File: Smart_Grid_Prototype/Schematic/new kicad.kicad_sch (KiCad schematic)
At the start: 70 parts, among them J1 EXT_POW, J2 24VAC _LOAD, J3 AC_INPUT, J4 DC_LOAD, J5 POW_SHARE, Q1 BD139, Q2 BD139, Q3 BD139, Q4 BD139, Q5 BD139, Q6 BD139, Q7 BD139, U1 ZC563900, U10 MODERATE_V, U11 HIGH_V, U12 PC817, U13 PC817, U14 PC817, U15 PC817, U16 PC817, U2 CKT_1_POWER_CON, U3 CKT_1_POWER_CON, U4 MIN_V, U5 LM7824_TO220, U6 MODERATE_V, U7 PC817, U8 LM317_TO-220, U9 MIN_V

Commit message: pcb updated with accrate component names
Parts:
- D1: value 1N5408/RELAY_FWD -> 1N5408/DIODE
- D2: value 1N5408/RELAY-1_FWD -> 1N5408/DIODE
- D3: value GBU4A -> GBU4A/BRIDGE_RECT
- D7: value LOAD_INDICATOR -> LOAD_STATUS
- R11, R2, R4, R5, R6, R7, R9: value 220 -> 220R
- R14: value 1.5kR -> 1.5k
- R15: value 2kR -> 2k
- R23, R24, R26, R3, R31: value 1 -> 1R
- R27: value 150 -> 150R
- U1: value ZC563900 -> ESP8266
- U10, U6: value MODERATE_V -> PC817
- U11: value HIGH_V -> PC817
- U2: value CKT_1_POWER_CON -> RELAY_INT
- U3: value CKT_1_POWER_CON -> RELAY_PS
- U4, U9: value MIN_V -> PC817
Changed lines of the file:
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@@
 			)
 		)
-		(property "Value" "1N5408/RELAY-1_FWD"
+		(property "Value" "1N5408/DIODE"
 			(at 38.608 83.82 90)
 			(effects
@@
 			)
 		)
-		(property "Value" "CKT_1_POWER_CON"
+		(property "Value" "RELAY_PS"
 			(at 77.47 69.85 0)
 			(effects
@@
 			)
 		)
-		(property "Value" "2kR"
+		(property "Value" "2k"
 			(at 176.53 149.86 90)
 			(effects
@@
 			)
 		)
-		(property "Value" "MODERATE_V"
+		(property "Value" "PC817"
 			(at 154.178 131.826 0)
 			(effects
@@
 			)
 		)
-		(property "Value" "1"
+		(property "Value" "1R"
 			(at 238.76 57.1499 0)
 			(effects
@@
 			)
 		)
-		(property "Value" "1N5408/RELAY_FWD"
+		(property "Value" "1N5408/DIODE"
 			(at 33.528 119.38 90)
 			(effects
@@
 			)
 		)
-		(property "Value" "MIN_V"
+		(property "Value" "PC817"
 			(at 154.178 111.506 0)
 			(effects
@@
 			)
 		)
-		(property "Value" "150"
+		(property "Value" "150R"
 			(at 265.43 113.284 0)
 			(effects
@@
 			)
 		)
-		(property "Value" "MODERATE_V"
+		(property "Value" "PC817"
 			(at 156.972 171.704 0)
 			(effects
@@
 			)
 		)
-		(property "Value" "ZC563900"
+		(property "Value" "ESP8266"
 			(at 18.542 142.748 0)
 			(effects
@@
 			)
 		)
-		(property "Value" "1.5kR"
+		(property "Value" "1.5k"
 			(at 176.53 135.89 90)
 			(effects
@@
 			)
 		)
-		(property "Value" "1"
+		(property "Value" "1R"
 			(at 251.46 57.1499 0)
 			(effects
@@
 			)
 		)
-		(property "Value" "220"
+		(property "Value" "220R"
 			(at 144.78 149.86 90)
 			(effects
@@
 			)
 		)
-		(property "Value" "220"
+		(property "Value" "220R"
 			(at 100.838 187.452 90)
 			(effects
@@
 			)
 		)
-		(property "Value" "1"
+		(property "Value" "1R"
 			(at 262.89 57.1499 0)
 			(effects
@@
 			)
 		)
-		(property "Value" "220"
+		(property "Value" "220R"
 			(at 144.78 135.89 90)
 			(effects
@@
 			)
 		)
-		(property "Value" "220"
+		(property "Value" "220R"
 			(at 139.7 189.23 90)
 			(effects
@@
 			)
 		)
-		(property "Value" "1"
+		(property "Value" "1R"
 			(at 274.32 57.1499 0)
 			(effects
@@
 			)
 		)
-		(property "Value" "MIN_V"
+		(property "Value" "PC817"
 			(at 102.108 175.006 0)
 			(effects
@@
 			)
 		)
-		(property "Value" "LOAD_INDICATOR"
+		(property "Value" "LOAD_STATUS"
 			(at 265.938 71.882 0)
 			(effects
@@
 			)
 		)
-		(property "Value" "1"
+		(property "Value" "1R"
 			(at 107.95 119.3799 0)
 			(effects
@@
 			)
 		)
-		(property "Value" "CKT_1_POWER_CON"
+		(property "Value" "RELAY_INT"
 			(at 71.12 105.41 0)
 			(effects
@@
 		(fields_autoplaced yes)
 		(property "Reference" "D3"
-			(at 62.23 29.1398 0)
+			(at 68.58 29.1398 0)
 			(effects
 				(font
@@
 			)
 		)
-		(property "Value" "GBU4A"
-			(at 62.23 31.6798 0)
+		(property "Value" "GBU4A/BRIDGE_RECT"
+			(at 68.58 31.6798 0)
 			(effects
 				(font
@@
 			)
 		)
-		(property "Value" "220"
+		(property "Value" "220R"
 			(at 144.78 109.22 90)
 			(effects
@@
 			)
 		)
-		(property "Value" "HIGH_V"
+		(property "Value" "PC817"
 			(at 154.178 152.146 0)
 			(effects
@@
 			)
 		)
-		(property "Value" "220"
+		(property "Value" "220R"
 			(at 161.29 48.2599 0)
 			(effects
@@
 			)
 		)
-		(property "Value" "220"
+		(property "Value" "220R"
 			(at 165.1 38.0999 0)
 			(effects

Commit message: Modified
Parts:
- renumbered R17 to R16, R18 to R17, R16 to R18
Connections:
- net EXT_POWER: now also U1.15 (VIN)
- no-connect marks 14 -> 13
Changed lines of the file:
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@@
 	)
 	(no_connect
-		(at 24.13 146.05)
-	)
-	(no_connect
 		(at 24.13 171.45)
 	)
@@
 	(wire
 		(pts
+			(xy 19.05 146.05) (xy 24.13 146.05)
+		)
+		(stroke
+			(width 0)
+			(type default)
+		)
+	)
+	(wire
+		(pts
 			(xy 193.04 36.83) (xy 196.85 36.83)
 		)
@@
 		)
 	)
+	(label "EXT_POWER"
+		(at 19.05 146.05 0)
+		(fields_autoplaced yes)
+		(effects
+			(font
+				(size 1.27 1.27)
+			)
+			(justify left bottom)
+		)
+	)
 	(label "1k_R"
 		(at 243.84 118.11 180)
@@
 		(on_board yes)
 		(dnp no)
-		(property "Reference" "R18"
+		(property "Reference" "R17"
 			(at 199.136 39.37 0)
 			(effects
@@
 			(project "new kicad"
 				(path "/e03aa56c-38cd-4df1-a477-6f5e62efd874"
-					(reference "R18")
+					(reference "R17")
 					(unit 1)
 				)
@@
 		(on_board yes)
 		(dnp no)
-		(property "Reference" "R17"
+		(property "Reference" "R16"
 			(at 199.136 26.67 0)
 			(effects
@@
 			(project "new kicad"
 				(path "/e03aa56c-38cd-4df1-a477-6f5e62efd874"
-					(reference "R17")
+					(reference "R16")
 					(unit 1)
 				)
@@
 		(on_board yes)
 		(dnp no)
-		(property "Reference" "R16"
+		(property "Reference" "R18"
 			(at 195.834 87.884 90)
 			(effects
@@
 			(project "new kicad"
 				(path "/e03aa56c-38cd-4df1-a477-6f5e62efd874"
-					(reference "R16")
+					(reference "R18")
 					(unit 1)
 				)

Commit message: updated
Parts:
- renumbered R18 to R16, R16 to R17, R17 to R18
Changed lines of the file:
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@@
 	(wire
 		(pts
-			(xy 19.05 146.05) (xy 24.13 146.05)
-		)
-		(stroke
-			(width 0)
-			(type default)
-		)
-	)
-	(wire
-		(pts
 			(xy 193.04 36.83) (xy 196.85 36.83)
 		)
@@
 		)
 	)
-	(label "EXT_POWER"
-		(at 19.05 146.05 0)
-		(fields_autoplaced yes)
-		(effects
-			(font
-				(size 1.27 1.27)
-			)
-			(justify left bottom)
-		)
-	)
 	(label "1k_R"
 		(at 243.84 118.11 180)
@@
 		)
 	)
+	(label "EXT_POWER"
+		(at 24.13 146.05 180)
+		(effects
+			(font
+				(size 1.27 1.27)
+			)
+			(justify right bottom)
+		)
+	)
 	(label "D5"
 		(at 73.66 158.75 0)
@@
 		(on_board yes)
 		(dnp no)
-		(property "Reference" "R17"
+		(property "Reference" "R18"
 			(at 199.136 39.37 0)
 			(effects
@@
 			(project "new kicad"
 				(path "/e03aa56c-38cd-4df1-a477-6f5e62efd874"
-					(reference "R17")
+					(reference "R18")
 					(unit 1)
 				)
@@
 		(on_board yes)
 		(dnp no)
-		(property "Reference" "R16"
+		(property "Reference" "R17"
 			(at 199.136 26.67 0)
 			(effects
@@
 			(project "new kicad"
 				(path "/e03aa56c-38cd-4df1-a477-6f5e62efd874"
-					(reference "R16")
+					(reference "R17")
 					(unit 1)
 				)
@@
 		(on_board yes)
 		(dnp no)
-		(property "Reference" "R18"
+		(property "Reference" "R16"
 			(at 195.834 87.884 90)
 			(effects
@@
 			(project "new kicad"
 				(path "/e03aa56c-38cd-4df1-a477-6f5e62efd874"
-					(reference "R18")
+					(reference "R16")
 					(unit 1)
 				)

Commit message: not good
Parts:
- added J4: USB4085-GF-A_REVB, USB4085-GF-A_REVB:GCT_USB4085-GF-A_REVB, symbol USB4085-GF-A_REVB:USB4085-GF-A_REVB
- added R1, R2: 5.1k, Resistor_THT:R_Axial_DIN0207_L6.3mm_D2.5mm_P15.24mm_Horizontal, symbol Device:R
- renumbered J4 to J5, J5 to J6, R8 to R10, R9 to R11, R10 to R12, R11 to R13, R12 to R14, R13 to R15, R14 to R16, R15 to R17, R17 to R18, R18 to R19, R16 to R20, R19 to R21, R20 to R22, R21 to R23, R22 to R24, R23 to R25, R24 to R26, R25 to R27, R26 to R28, R27 to R29, R1 to R3, R28 to R30, R29 to R31, R30 to R32, R31 to R33, R2 to R4, R3 to R5, R4 to R6, R5 to R7, R6 to R8, R7 to R9
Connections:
- net EXT_POWER: now also J4.A4 (VBUS), J4.A9 (VBUS), J4.B4 (VBUS), J4.B9 (VBUS)
- net GND: now also J4.A1 (GND), J4.A12 (GND), J4.B1 (GND), J4.B12 (GND), J4.S1 (SHELL), J4.S2 (SHELL), J4.S3 (SHELL), J4.S4 (SHELL), R1.1, R2.1
- new net CC1: J4.A5 (CC1), R1.2
- new net CC2: J4.B5 (CC2), R2.2
- no-connect marks 13 -> 19

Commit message: error
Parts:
- removed J4: USB4085-GF-A_REVB, USB4085-GF-A_REVB:GCT_USB4085-GF-A_REVB, symbol USB4085-GF-A_REVB:USB4085-GF-A_REVB
- added J4: USB_C_Receptacle_PowerOnly_6P, Connector_USB:USB_C_Receptacle_GCT_USB4125-xx-x-0190_6P_TopMnt_Horizontal, symbol Connector:USB_C_Receptacle_PowerOnly_6P
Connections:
- net CC1: now also J4.A5 (CC1)
- net CC2: now also J4.B5 (CC2)
- net GND: now also J4.A12 (GND), J4.B12 (GND), J4.S1 (SHIELD)
- net EXT_POWER renamed VCC
- net VCC: now also J4.A9 (VBUS), J4.B9 (VBUS)
- no-connect marks 19 -> 13

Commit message: Perfect PCB
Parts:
- removed J4: USB_C_Receptacle_PowerOnly_6P, Connector_USB:USB_C_Receptacle_GCT_USB4125-xx-x-0190_6P_TopMnt_Horizontal, symbol Connector:USB_C_Receptacle_PowerOnly_6P
- removed R1, R2: 5.1k, Resistor_THT:R_Axial_DIN0207_L6.3mm_D2.5mm_P15.24mm_Horizontal, symbol Device:R
- added J6: USB_C_Receptacle_PowerOnly_6P, Connector_USB:USB_C_Receptacle_GCT_USB4125-xx-x-0190_6P_TopMnt_Horizontal, symbol Connector:USB_C_Receptacle_PowerOnly_6P
- added R32, R33: 5.1k, Resistor_THT:R_Axial_DIN0207_L6.3mm_D2.5mm_P15.24mm_Horizontal, symbol Device:R
- renumbered J5 to J4, J6 to J5, R3 to R1, R12 to R10, R13 to R11, R14 to R12, R15 to R13, R16 to R14, R17 to R15, R20 to R16, R18 to R17, R19 to R18, R21 to R19, R4 to R2, R22 to R20, R23 to R21, R24 to R22, R25 to R23, R26 to R24, R27 to R25, R28 to R26, R29 to R27, R30 to R28, R31 to R29, R5 to R3, R32 to R30, R33 to R31, R6 to R4, R7 to R5, R8 to R6, R9 to R7, R10 to R8, R11 to R9
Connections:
- net GND: now also J6.A12 (GND), J6.B12 (GND), J6.S1 (SHIELD), R32.1, R33.2
- net VCC: now also J6.A9 (VBUS), J6.B9 (VBUS)
- new net: J6.A5 (CC1), R32.2
- new net: J6.B5 (CC2), R33.1
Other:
- moved on the sheet: C1, C2, C3, C4, D1, D2, D3, D4, D5, D6, D7, J1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

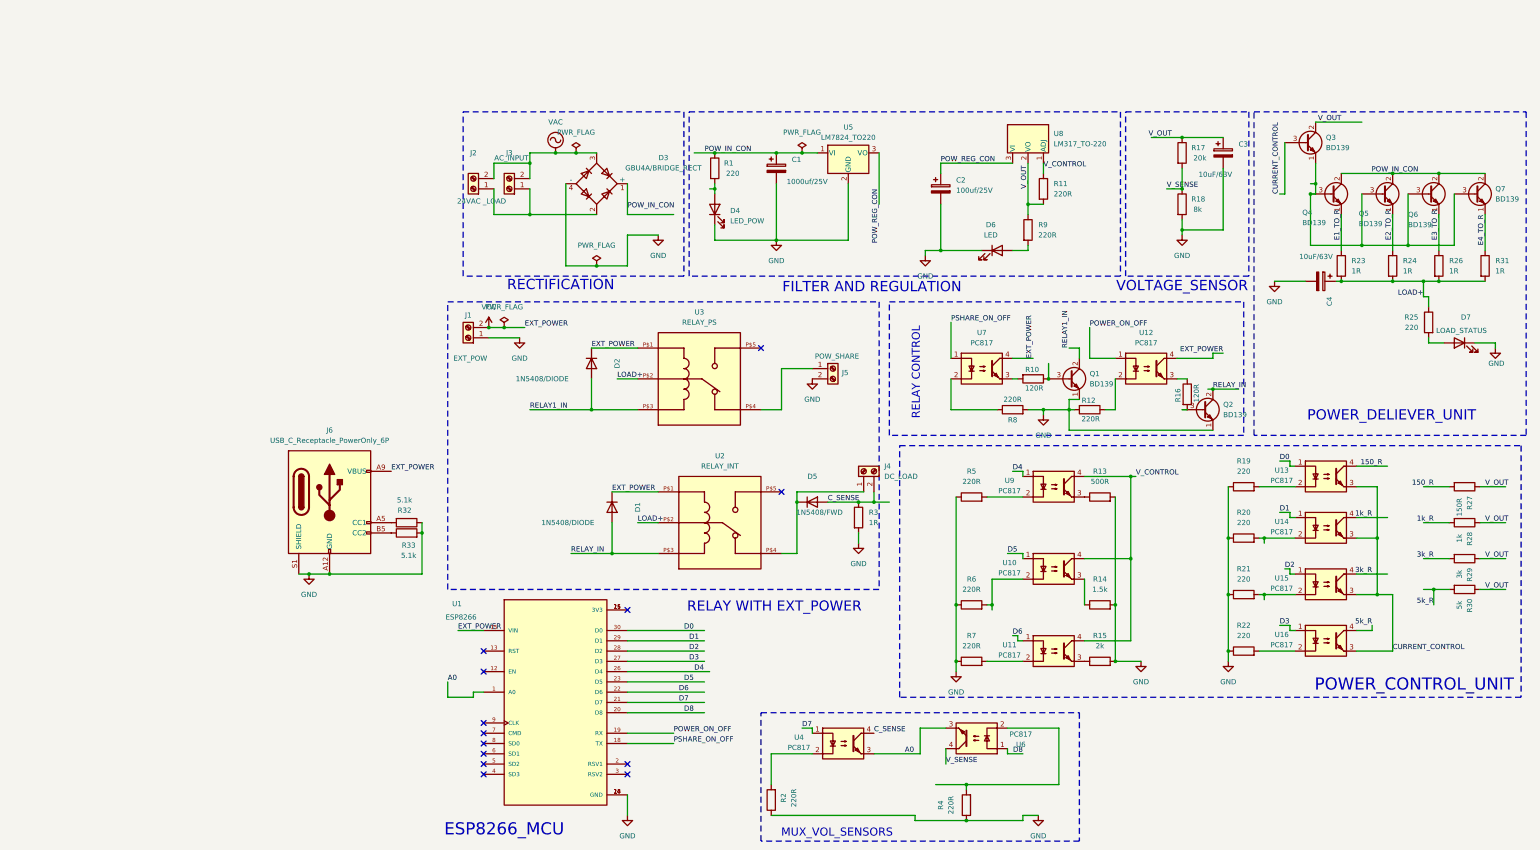
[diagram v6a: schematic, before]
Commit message: ac load switch added
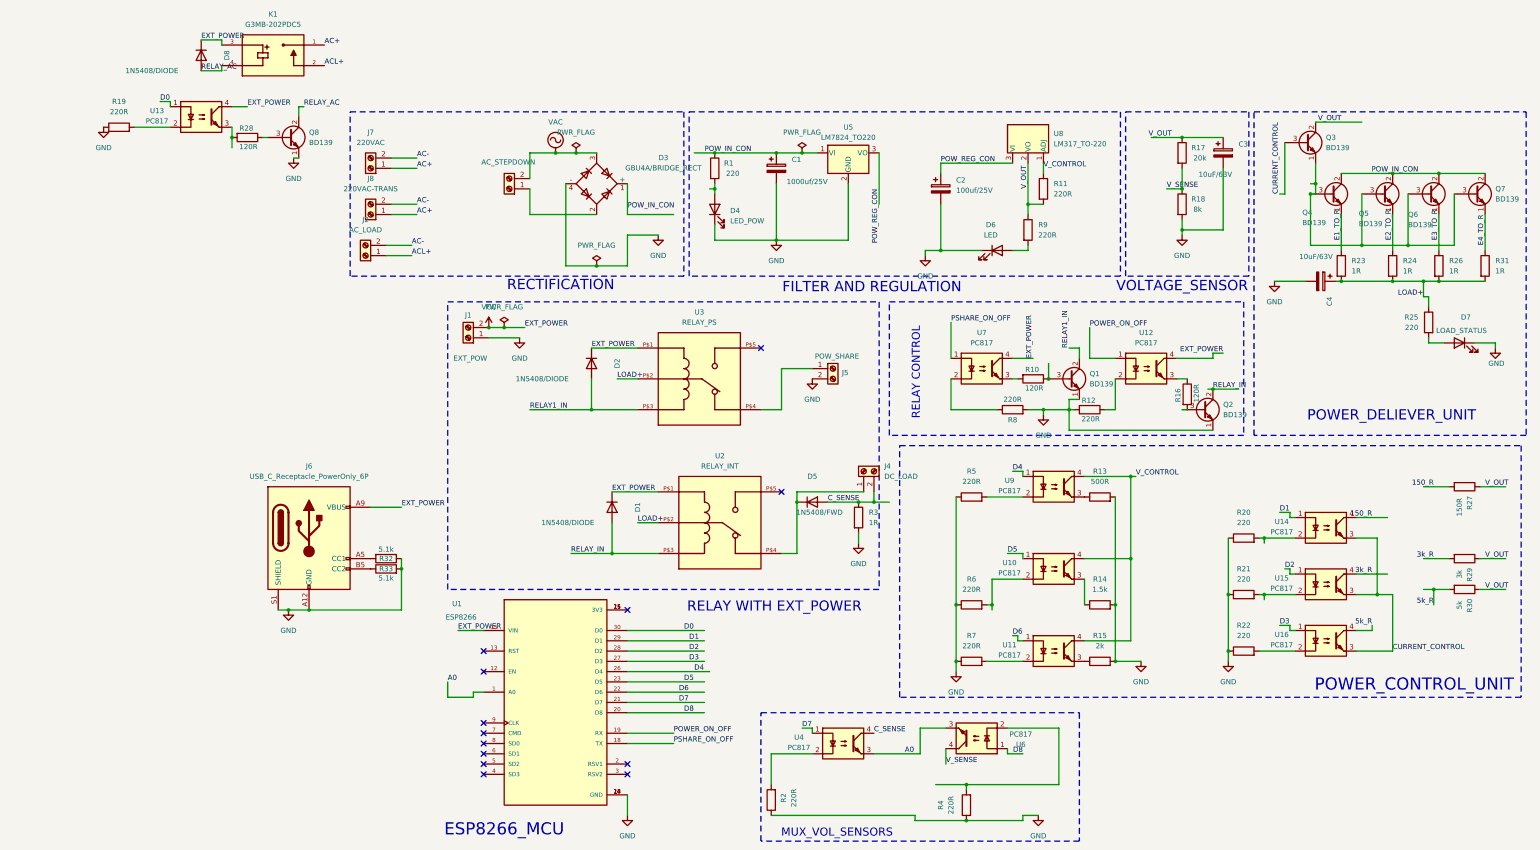
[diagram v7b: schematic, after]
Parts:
- added D8: 1N5408/DIODE, Diode_THT:D_5W_P12.70mm_Horizontal, symbol Device:D
- added J7: 220VAC, TerminalBlock_4Ucon:TerminalBlock_4Ucon_1x02_P3.50mm_Horizontal, symbol Connector:Screw_Terminal_01x02
- added J8: 220VAC-TRANS, TerminalBlock_4Ucon:TerminalBlock_4Ucon_1x02_P3.50mm_Horizontal, symbol Connector:Screw_Terminal_01x02
- added K1: G3MB-202PDC5, Library:RELAY_G3MB-202PDC5, symbol G3MB-202PDC5:G3MB-202PDC5
- added Q8: BD139, Package_TO_SOT_THT:TO-126-3_Vertical, symbol Transistor_BJT:BD139
- J2: value 24VAC _LOAD -> AC_LOAD
- J3: value AC_INPUT -> AC_STEPDOWN
- R19: value 220 -> 220R
- R28: value 1k -> 120R
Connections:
- net 150_R: now also U14.4; no longer U13.4
- net CURRENT_CONTROL: no longer U13.3
- net GND: now also Q8.1 (E)
- net VAC: no longer J2.2 (Pin_2)
- net VCC: now also U13.4, D8.1 (K), K1.3
- net V_OUT: no longer R28.1
- net at D3.2, J3.1 (Pin_1): no longer J2.1 (Pin_1)
- net 1k_R: no longer names the net of R28.2
- net 1k_R: now also U13.3; no longer U14.4
- new net: Q8.3 (B), R28.1
- new net AC+: J7.1 (Pin_1), J8.1 (Pin_1), K1.1
- new net AC-: J2.2 (Pin_2), J7.2 (Pin_2), J8.2 (Pin_2)
- new net ACL+: J2.1 (Pin_1), K1.2
- new net RELAY_AC: D8.2 (A), K1.4, Q8.2 (C)
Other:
- moved on the sheet: J6, R32, R33

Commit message: finalised
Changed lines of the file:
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@@
 	)
 	(junction
+		(at 69.85 166.37)
+		(diameter 0)
+		(color 0 0 0 0)
+	)
+	(junction
 		(at 139.7 81.28)
 		(diameter 0)
@@
 	)
 	(junction
-		(at 68.58 166.37)
-		(diameter 0)
-		(color 0 0 0 0)
-	)
-	(junction
 		(at 328.93 76.2)
 		(diameter 0)
@@
 	(wire
 		(pts
+			(xy 85.09 153.67) (xy 83.82 153.67)
+		)
+		(stroke
+			(width 0)
+			(type default)
+		)
+	)
+	(wire
+		(pts
 			(xy 323.85 68.58) (xy 323.85 77.47)
 		)
@@
 	(wire
 		(pts
+			(xy 85.09 156.21) (xy 83.82 156.21)
+		)
+		(stroke
+			(width 0)
+			(type default)
+		)
+	)
+	(wire
+		(pts
 			(xy 231.14 210.82) (xy 231.14 209.55)
 		)
@@
 	(wire
 		(pts
-			(xy 63.5 166.37) (xy 68.58 166.37)
-		)
-		(stroke
-			(width 0)
-			(type default)
-		)
-	)
-	(wire
-		(pts
 			(xy 294.64 72.39) (xy 284.48 72.39)
 		)
@@
 	(wire
 		(pts
+			(xy 69.85 166.37) (xy 91.44 166.37)
+		)
+		(stroke
+			(width 0)
+			(type default)
+		)
+	)
+	(wire
+		(pts
 			(xy 356.87 100.33) (xy 361.95 100.33)
 		)
@@
 	(wire
 		(pts
-			(xy 83.82 140.97) (xy 91.44 140.97)
+			(xy 85.09 140.97) (xy 91.44 140.97)
 		)
 		(stroke
@@
 	(wire
 		(pts
-			(xy 60.96 166.37) (xy 63.5 166.37)
+			(xy 62.23 166.37) (xy 63.5 166.37)
 		)
 		(stroke
@@
 	(wire
 		(pts
-			(xy 91.44 166.37) (xy 68.58 166.37)
+			(xy 63.5 166.37) (xy 69.85 166.37)
 		)
 		(stroke
@@
 		)
 		(property "Value" "GND"
-			(at 120.65 104.14 0)
+			(at 123.19 100.3299 0)
 			(effects
 				(font
 					(size 1.27 1.27)
 				)
+				(justify left)
 			)
 		)
@@
 		(on_board yes)
 		(dnp no)
-		(fields_autoplaced yes)
 		(property "Reference" "#PWR017"
 			(at 113.03 100.33 0)
@@
 		)
 		(property "Value" "VCC"
-			(at 113.03 91.44 0)
+			(at 113.03 91.694 0)
 			(effects
 				(font
 					(size 1.27 1.27)
 				)
+				(justify left)
 			)
 		)
@@
 		(on_board yes)
 		(dnp no)
-		(fields_autoplaced yes)
 		(property "Reference" "#FLG04"
 			(at 116.84 94.615 0)
@@
 		)
 		(property "Value" "PWR_FLAG"
-			(at 116.84 91.44 0)
+			(at 120.65 92.456 0)
 			(effects
 				(font
 					(size 1.27 1.27)
 				)
+				(justify left)
 			)
 		)
@@
 	)
 	(symbol
-		(lib_id "Connector:USB_C_Receptacle_PowerOnly_6P")
-		(at 68.58 148.59 0)
-		(unit 1)
-		(exclude_from_sim no)
-		(in_bom yes)
-		(on_board yes)
-		(dnp no)
-		(fields_autoplaced yes)
-		(property "Reference" "J6"
-			(at 68.58 130.81 0)
-			(effects
-				(font
-					(size 1.27 1.27)
-				)
-			)
-		)
-		(property "Value" "USB_C_Receptacle_PowerOnly_6P"
-			(at 68.58 133.35 0)
-			(effects
-				(font
-					(size 1.27 1.27)
-				)
-			)
-		)
-		(property "Footprint" "Connector_USB:USB_C_Receptacle_GCT_USB4125-xx-x-0190_6P_TopMnt_Horizontal"
-			(at 72.39 146.05 0)
-			(effects
-				(font
-					(size 1.27 1.27)
-				)
-				(hide yes)
-			)
-		)
-		(property "Datasheet" "https://www.usb.org/sites/default/files/documents/usb_type-c.zip"
-			(at 68.58 148.59 0)
-			(effects
-				(font
-					(size 1.27 1.27)
-				)
-				(hide yes)
-			)
-		)
-		(property "Description" "USB Power-Only 6P Type-C Receptacle connector"
-			(at 68.58 148.59 0)
-			(effects
-				(font
-					(size 1.27 1.27)
-				)
-				(hide yes)
-			)
-		)
-		(pin "S1"
-		)
-		(pin "B12"
-		)
-		(pin "B9"
-		)
-		(pin "B5"
-		)
-		(pin "A12"
-		)
-		(pin "A5"
-		)
-		(pin "A9"
-		)
-		(instances
-			(project ""
-				(path "/e03aa56c-38cd-4df1-a477-6f5e62efd874"
-					(reference "J6")
-					(unit 1)
-				)
-			)
-		)
-	)
-	(symbol
 		(lib_id "Device:R")
 		(at 53.34 49.53 270)
@@
 	)
 	(symbol
+		(lib_id "Connector:USB_C_Receptacle_PowerOnly_6P")
+		(at 69.85 148.59 0)
+		(unit 1)
+		(exclude_from_sim no)
+		(in_bom yes)
+		(on_board yes)
+		(dnp no)
+		(fields_autoplaced yes)
+		(property "Reference" "J6"
+			(at 69.85 130.81 0)
+			(effects
+				(font
+					(size 1.27 1.27)
+				)
+			)
+		)
+		(property "Value" "USB_C_Receptacle_PowerOnly_6P"
+			(at 69.85 133.35 0)
+			(effects
+				(font
+					(size 1.27 1.27)
+				)
+			)
+		)
+		(property "Footprint" "Connector_USB:USB_C_Receptacle_GCT_USB4125-xx-x-0190_6P_TopMnt_Horizontal"
+			(at 73.66 146.05 0)
+			(effects
+				(font
+					(size 1.27 1.27)
+				)
+				(hide yes)
+			)
+		)
+		(property "Datasheet" "https://www.usb.org/sites/default/files/documents/usb_type-c.zip"
+			(at 69.85 148.59 0)
+			(effects
+				(font
+					(size 1.27 1.27)
+				)
+				(hide yes)
+			)
+		)
+		(property "Description" "USB Power-Only 6P Type-C Receptacle connector"
+			(at 69.85 148.59 0)
+			(effects
+				(font
+					(size 1.27 1.27)
+				)
+				(hide yes)
+			)
+		)
+		(pin "B12"
+		)
+		(pin "B5"
+		)
+		(pin "A9"
+		)
+		(pin "A12"
+		)
+		(pin "B9"
+		)
+		(pin "S1"
+		)
+		(pin "A5"
+		)
+		(instances
+			(project ""
+				(path "/e03aa56c-38cd-4df1-a477-6f5e62efd874"
+					(reference "J6")
+					(unit 1)
+				)
+			)
+		)
+	)
+	(symbol
 		(lib_id "Device:R")
 		(at 168.91 57.15 0)
@@
 		(on_board yes)
 		(dnp no)
+		(fields_autoplaced yes)
 		(property "Reference" "J1"
-			(at 107.95 93.472 0)
+			(at 107.95 90.17 0)
 			(effects
 				(font
@@
 		)
 		(property "Value" "EXT_POW"
-			(at 108.458 104.14 0)
+			(at 107.95 92.71 0)
 			(effects
 				(font
